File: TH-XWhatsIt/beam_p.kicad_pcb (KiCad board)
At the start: 2 copper layers, 162.2 x 33.2 mm, 50 parts, among them J1 BEAMSPRING CONNECTOR, J3 EXPANSION HEADER, U1 MCP4921-EP, U2 LM339, U3 74HCT595, U4 74HCT595, U5 ProMicro, U7 74HCT595

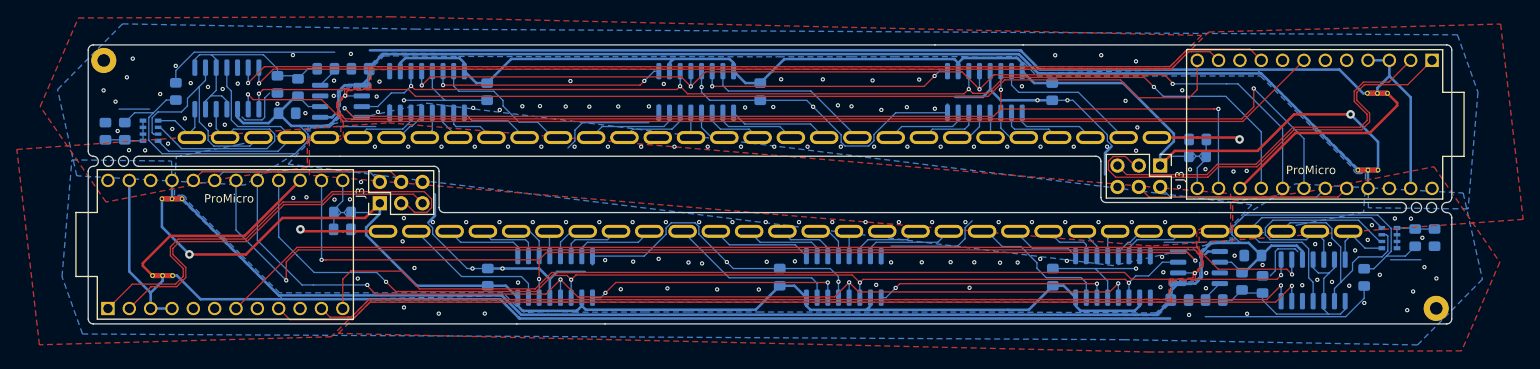
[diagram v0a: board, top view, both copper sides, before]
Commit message: added tooling holes to existing panel
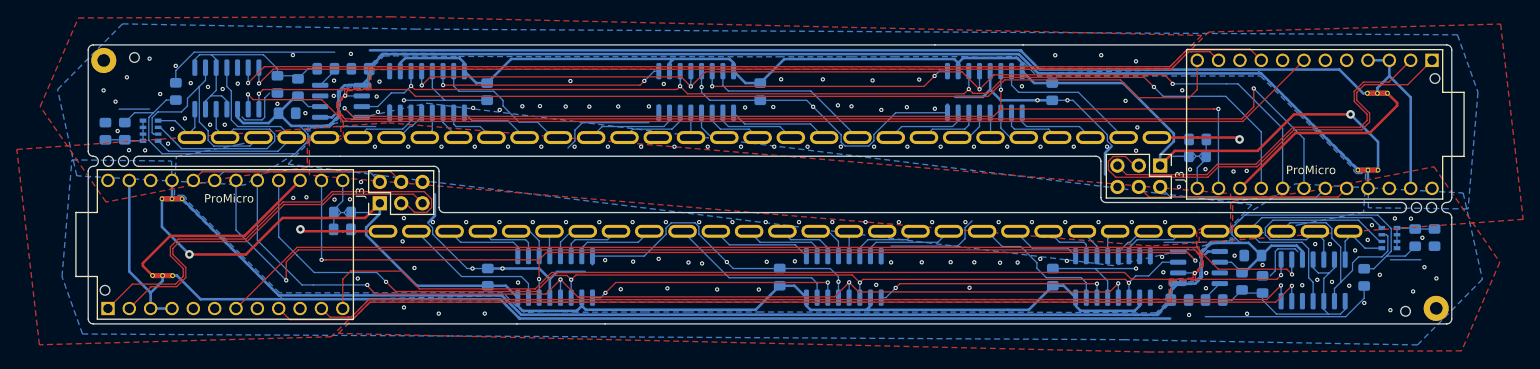
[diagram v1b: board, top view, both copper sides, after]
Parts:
- added REF**: tooling_hole, TH-XWhatsIt:tooling_hole, F.Cu at (271.8, 112.5)
- added REF**: tooling_hole, TH-XWhatsIt:tooling_hole, F.Cu at (113.5, 137.8)
- added REF**: tooling_hole, TH-XWhatsIt:tooling_hole, F.Cu at (268.2, 140.2)
- added REF**: tooling_hole, TH-XWhatsIt:tooling_hole, F.Cu at (117.0, 110.0)
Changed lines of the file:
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@@
   (general
     (thickness 1.6)
-    (drawings 55)
+    (drawings 59)
     (tracks 1206)
     (zones 0)
-    (modules 50)
+    (modules 54)
     (nets 61)
   )
@@
     (39 F.Mask user)
     (40 Dwgs.User user)
-    (41 Cmts.User user)
+    (41 Cmts.User user hide)
     (42 Eco1.User user)
     (43 Eco2.User user)
@@
     (diff_pair_gap 0.1524)
   )
+  (module TH-XWhatsIt:tooling_hole (layer F.Cu)
+    (at 271.75 112.55)
+    (fp_text reference REF** (at 0 -11.5) (layer F.SilkS) hide
+      (effects (font (size 1 1) (thickness 0.15)))
+    )
+    (fp_text value tooling_hole (at 0 -12.5) (layer F.Fab) hide
+      (effects (font (size 1 1) (thickness 0.15)))
+    )
+    (pad "" np_thru_hole circle (at 0 0) (size 1.152 1.152) (drill 1.152) (layers *.Cu *.Mask)
+      (solder_mask_margin 0.148))
+  )
+  (module TH-XWhatsIt:tooling_hole (layer F.Cu)
+    (at 113.5 137.75)
+    (fp_text reference REF** (at 0 -11.5) (layer F.SilkS) hide
+      (effects (font (size 1 1) (thickness 0.15)))
+    )
+    (fp_text value tooling_hole (at 0 -12.5) (layer F.Fab) hide
+      (effects (font (size 1 1) (thickness 0.15)))
+    )
+    (pad "" np_thru_hole circle (at 0 0) (size 1.152 1.152) (drill 1.152) (layers *.Cu *.Mask)
+      (solder_mask_margin 0.148))
+  )
+  (module TH-XWhatsIt:tooling_hole (layer F.Cu)
+    (at 268.25 140.25)
+    (fp_text reference REF** (at 0 -11.5) (layer F.SilkS) hide
+      (effects (font (size 1 1) (thickness 0.15)))
+    )
+    (fp_text value tooling_hole (at 0 -12.5) (layer F.Fab) hide
+      (effects (font (size 1 1) (thickness 0.15)))
+    )
+    (pad "" np_thru_hole circle (at 0 0) (size 1.152 1.152) (drill 1.152) (layers *.Cu *.Mask)
+      (solder_mask_margin 0.148))
+  )
+  (module TH-XWhatsIt:tooling_hole (layer F.Cu)
+    (at 117 110.05)
+    (fp_text reference REF** (at 0 -11.5) (layer F.SilkS) hide
+      (effects (font (size 1 1) (thickness 0.15)))
+    )
+    (fp_text value tooling_hole (at 0 -12.5) (layer F.Fab) hide
+      (effects (font (size 1 1) (thickness 0.15)))
+    )
+    (pad "" np_thru_hole circle (at 0 0) (size 1.152 1.152) (drill 1.152) (layers *.Cu *.Mask)
+      (solder_mask_margin 0.148))
+  )
   (module Connector_PinHeader_2.54mm:PinHeader_2x03_P2.54mm_Vertical (layer F.Cu)
     (at 146.19888 127.3929 90)
@@
     )
   )
+  (gr_poly (pts (xy 273.4 128.5) (xy 267.3 128.5) (xy 267.5 127.3) (xy 273.3 127.3)) (layer Cmts.User) (width 0.05))
+  (gr_poly (pts (xy 273.4 128.5) (xy 267.3 128.5) (xy 267.5 127.3) (xy 273.3 127.3)) (layer Cmts.User) (width 0.05))
+  (gr_poly (pts (xy 118.1 123) (xy 112 123) (xy 112.2 121.8) (xy 118 121.8)) (layer Cmts.User) (width 0.05))
+  (gr_poly (pts (xy 118.1 123) (xy 112 123) (xy 112.2 121.8) (xy 118 121.8)) (layer Cmts.User) (width 0.05))
   (gr_arc (start 267.75 127.9) (end 267.75 128.5) (angle -180) (layer Edge.Cuts) (width 0.05))
   (gr_arc (start 269.55 127.9) (end 269.55 127.3) (angle -180) (layer Edge.Cuts) (width 0.05))
@@
   (via (at 149.07162 139.79318) (size 0.508) (drill 0.254) (layers F.Cu B.Cu) (net 44))
   (via (at 249.394 140.53994) (size 0.508) (drill 0.254) (layers F.Cu B.Cu) (net 44))
-  (via (at 268.44908 140.11576) (size 0.508) (drill 0.254) (layers F.Cu B.Cu) (net 44))
+  (via (at 266.44908 140.11576) (size 0.508) (drill 0.254) (layers F.Cu B.Cu) (net 44))
   (via (at 269.15012 137.89072) (size 0.508) (drill 0.254) (layers F.Cu B.Cu) (net 44))
   (via (at 271.9238 136.33624) (size 0.508) (drill 0.254) (layers F.Cu B.Cu) (net 44))
@@
   (via (at 236.17838 110.50682) (size 0.508) (drill 0.254) (layers F.Cu B.Cu) (net 44))
   (via (at 135.856 109.76006) (size 0.508) (drill 0.254) (layers F.Cu B.Cu) (net 44))
-  (via (at 116.80092 110.18424) (size 0.508) (drill 0.254) (layers F.Cu B.Cu) (net 44))
+  (via (at 118.80092 110.18424) (size 0.508) (drill 0.254) (layers F.Cu B.Cu) (net 44))
   (via (at 116.09988 112.40928) (size 0.508) (drill 0.254) (layers F.Cu B.Cu) (net 44))
   (via (at 113.3262 113.96376) (size 0.508) (drill 0.254) (layers F.Cu B.Cu) (net 44))
@@
       )
     )
+  )
+  (zone (net 0) (net_name "") (layers F&B.Cu) (hatch edge 0.508)
+    (connect_pads (clearance 0.152))
+    (min_thickness 0.254)
+    (keepout (tracks not_allowed) (vias not_allowed) (copperpour not_allowed))
+    (fill (arc_segments 32) (thermal_gap 0.508) (thermal_bridge_width 0.508))
+    (polygon
+      (pts
+        (xy 273.55 128.5) (xy 266.55 128.5) (xy 266.65 127.3) (xy 273.45 127.3)
+      )
+    )

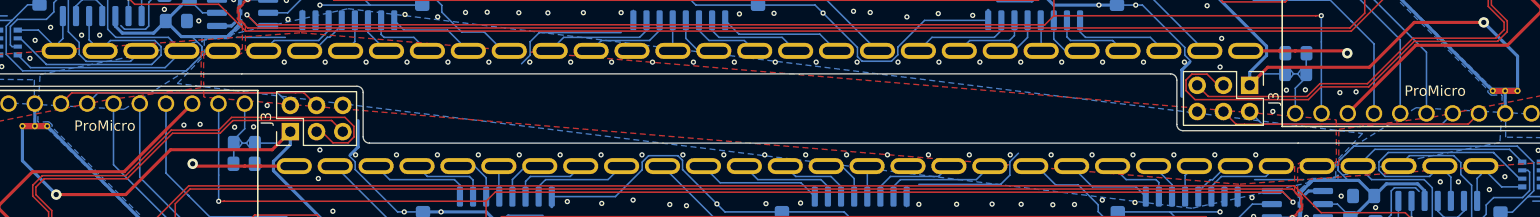
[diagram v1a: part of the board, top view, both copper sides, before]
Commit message: rotate silkscreens into proper orientation on panel
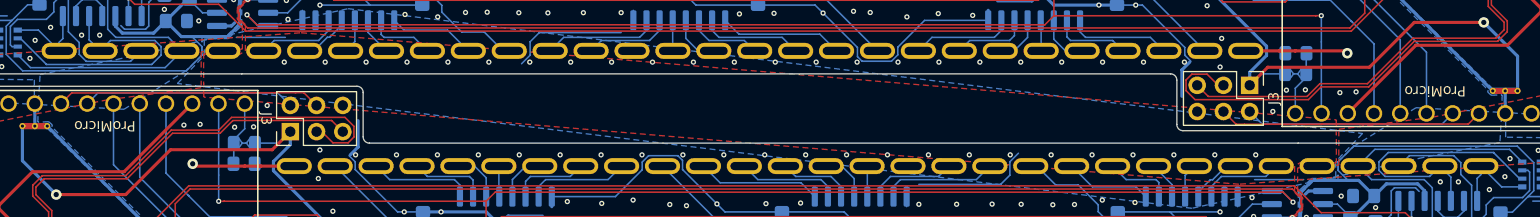
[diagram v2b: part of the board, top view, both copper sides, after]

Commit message: added lcsc numbers for remaining chips, changed some silkscreen to match parts, removed stay-upright flag from all silkscreen, etc...
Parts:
- U1 (x2): value MCP4921-EP -> MCP4921-E
- U2 (x2): value LM339 -> LM339A
- U3 (x2), U4 (x2), U7 (x2): value 74HCT595 -> 74AHC595

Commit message: added silkscreen for jlcpcb order number to panel
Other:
- board text added: "JLCJLCJLCJLC"
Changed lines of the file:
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@@
   (general
     (thickness 1.6)
-    (drawings 59)
+    (drawings 60)
     (tracks 1206)
     (zones 0)
@@
   (layers
     (0 F.Cu jumper)
-    (31 B.Cu signal)
-    (32 B.Adhes user)
-    (33 F.Adhes user)
-    (34 B.Paste user)
-    (35 F.Paste user)
-    (36 B.SilkS user)
+    (31 B.Cu signal hide)
+    (32 B.Adhes user hide)
+    (33 F.Adhes user hide)
+    (34 B.Paste user hide)
+    (35 F.Paste user hide)
+    (36 B.SilkS user hide)
     (37 F.SilkS user)
-    (38 B.Mask user)
-    (39 F.Mask user)
-    (40 Dwgs.User user)
-    (41 Cmts.User user)
-    (42 Eco1.User user)
-    (43 Eco2.User user)
-    (44 Edge.Cuts user)
-    (45 Margin user)
-    (46 B.CrtYd user)
-    (47 F.CrtYd user)
-    (48 B.Fab user)
-    (49 F.Fab user)
+    (38 B.Mask user hide)
+    (39 F.Mask user hide)
+    (40 Dwgs.User user hide)
+    (41 Cmts.User user hide)
+    (42 Eco1.User user hide)
+    (43 Eco2.User user hide)
+    (44 Edge.Cuts user hide)
+    (45 Margin user hide)
+    (46 B.CrtYd user hide)
+    (47 F.CrtYd user hide)
+    (48 B.Fab user hide)
+    (49 F.Fab user hide)
   )
   (setup
@@
     )
   )
+  (gr_text JLCJLCJLCJLC (at 201.25 134.4) (layer F.SilkS)
+    (effects (font (size 1 1) (thickness 0.15)))
+  )
   (gr_poly (pts (xy 273.4 128.5) (xy 267.3 128.5) (xy 267.5 127.3) (xy 273.3 127.3)) (layer Cmts.User) (width 0.05))

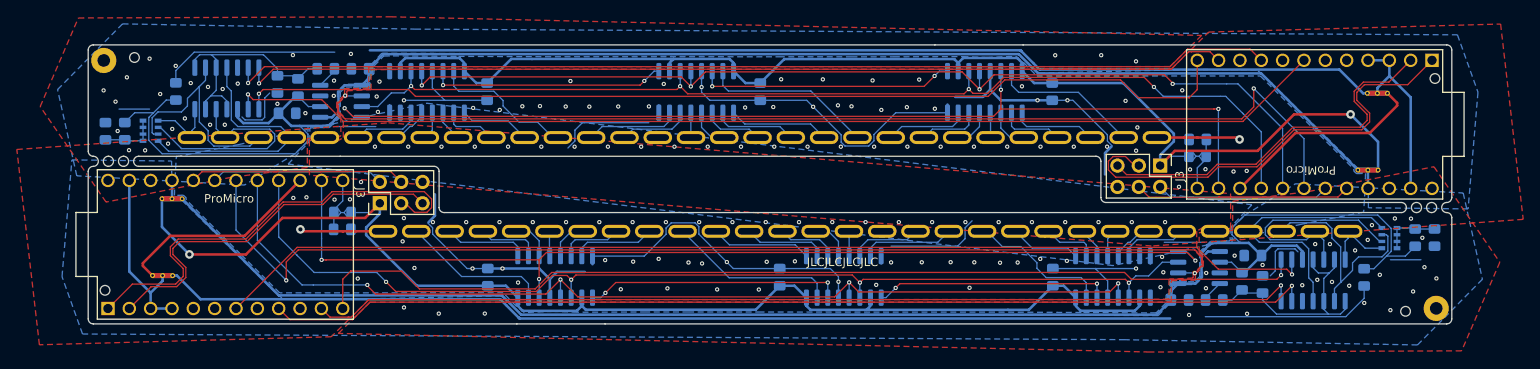
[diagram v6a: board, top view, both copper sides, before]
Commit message: panel: tightened up and fixed copper fills, changed net tie to solid clearance
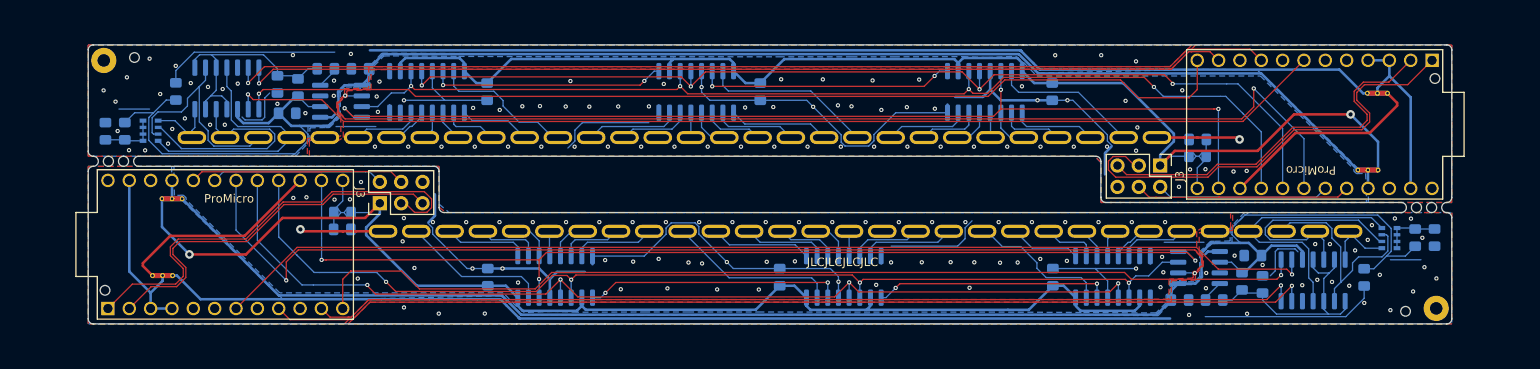
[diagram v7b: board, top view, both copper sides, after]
